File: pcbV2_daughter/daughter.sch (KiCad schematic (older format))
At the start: 27 parts, among them J3 Conn_01x03_Male, J6 Conn_01x03_Male

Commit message: finished v1 of daughter board
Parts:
- J6: footprint (none) -> Connector_PinHeader_2.54mm:PinHeader_1x03_P2.54mm_Vertical
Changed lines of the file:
@@
 F 0 "J6" H 15458 9581 50  0000 C CNN
 F 1 "Conn_01x03_Male" H 15458 9490 50  0000 C CNN
-F 2 "" H 15350 9300 50  0001 C CNN
+F 2 "Connector_PinHeader_2.54mm:PinHeader_1x03_P2.54mm_Vertical" H 15350 9300 50  0001 C CNN
 F 3 "~" H 15350 9300 50  0001 C CNN
 	1    15350 9300

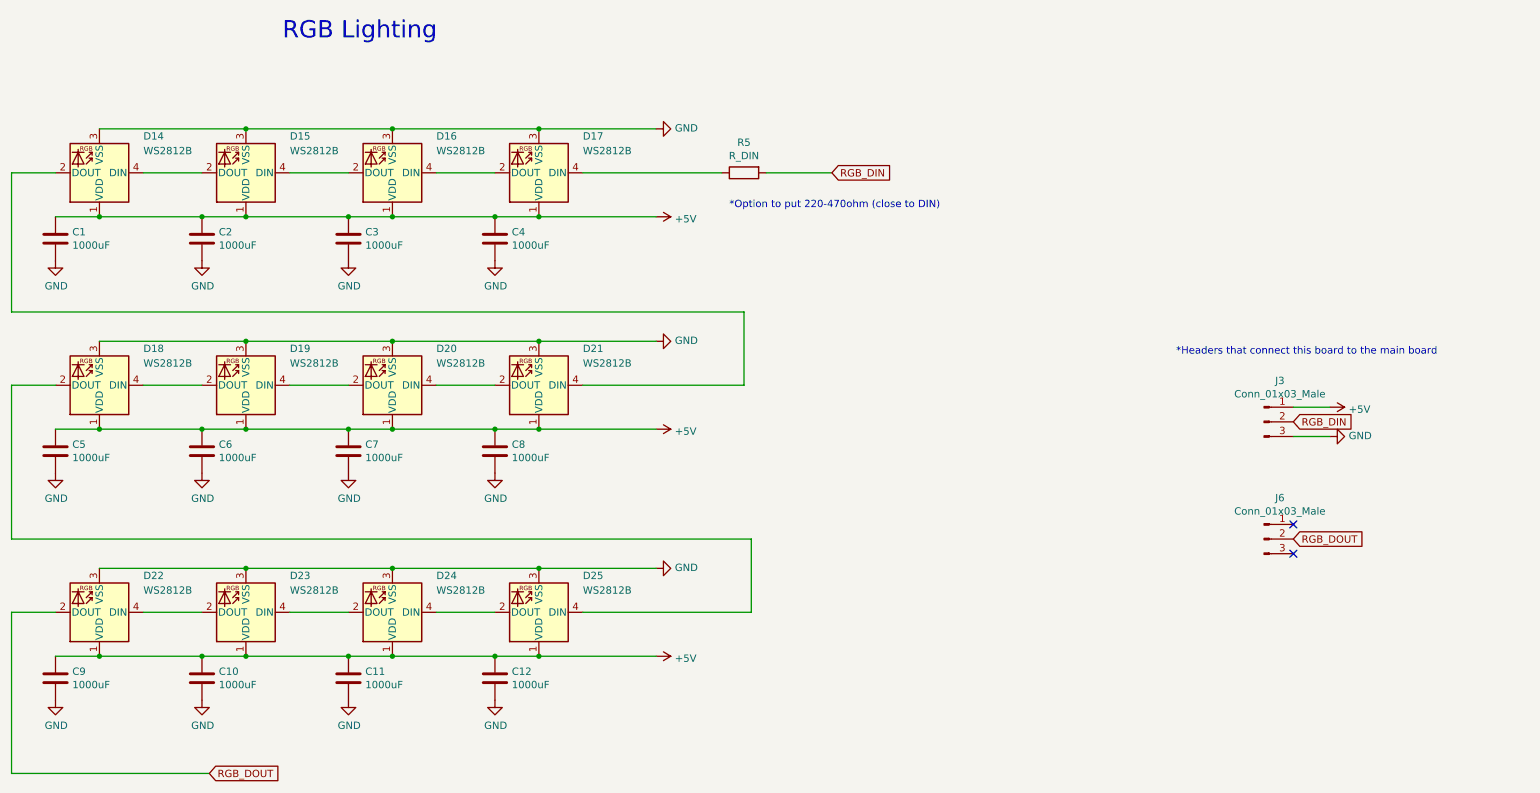
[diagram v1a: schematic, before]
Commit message: Prototype 1 Code changes (#9)
* started working on low priority work thread

* removed usb c

* setup a low priority worker thread that we can assign a bunch of menial tasks to

* added dip switch support

* started rewiring

* v2 layout

* edited layout, updated daughter board

* moved some labels around

* generated plots files

* added the ability to enable, disable and delete threads by handler ID

* added thread safety to the low priority work thread

* added documentation for dip switches

* finished adding thread safety code, fixed SPI dma ram waste usage

* update

* updated gerber files

* moved over lpwork into it's own module

* added signature to the codebase

* added more signatures

* updating daughter board to be more structurally safe

* generated gerber files

Co-authored-by: Jonathan Low <jwlow@uci.edu>
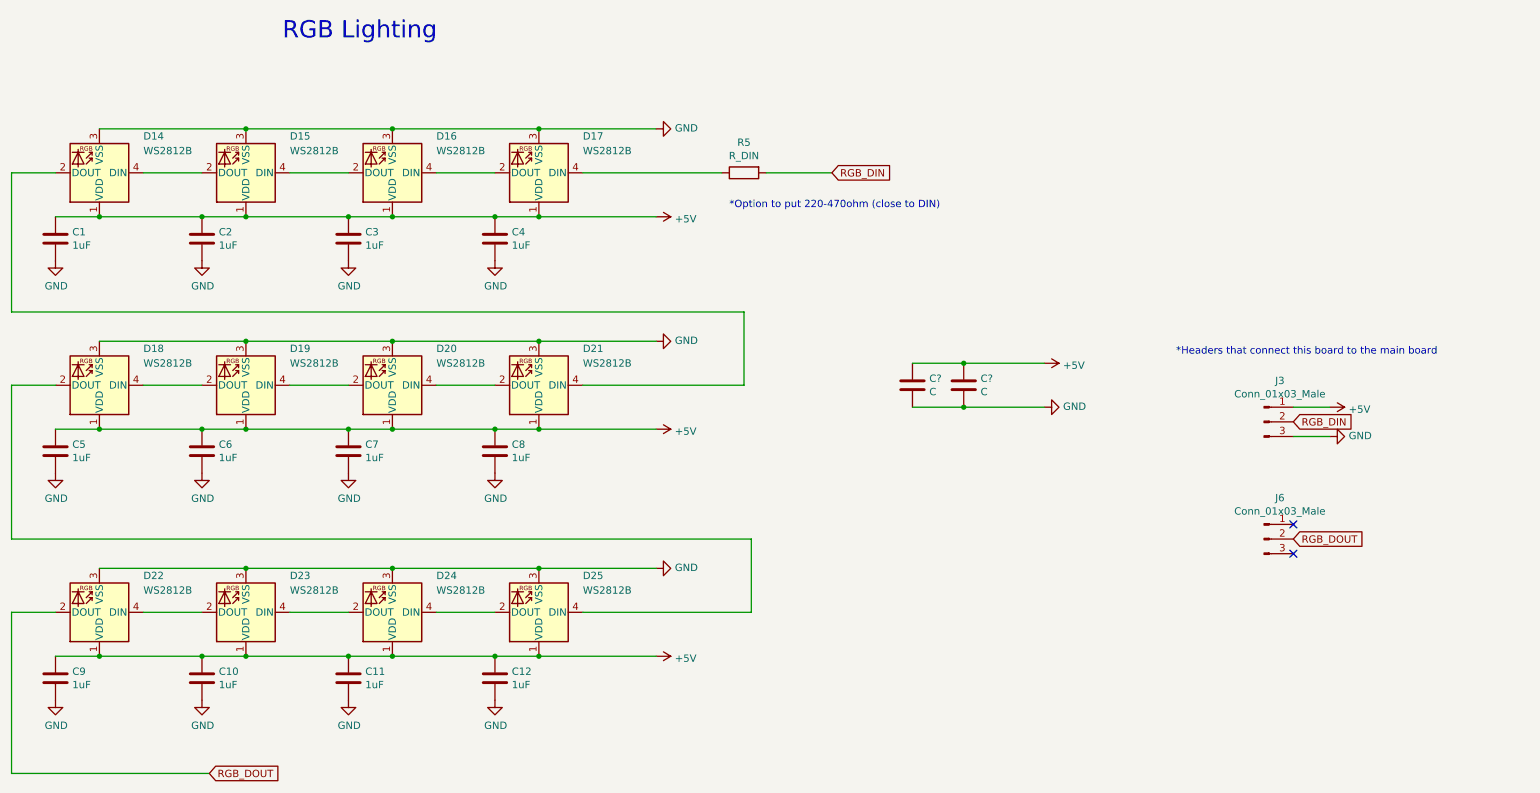
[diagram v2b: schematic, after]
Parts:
- added C? (x2): C, symbol Device:C
- C1, C10, C11, C12, C2, C3, C4, C5, C6, C7, C8, C9: value 1000uF -> 1uF
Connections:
- net +5V: now also C?.1, C?.1
- net GND: now also C?.2, C?.2
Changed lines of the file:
@@
 P 7100 7250
 F 0 "C1" H 7215 7296 50  0000 L CNN
-F 1 "1000uF" H 7215 7205 50  0000 L CNN
+F 1 "1uF" H 7215 7205 50  0000 L CNN
 F 2 "Capacitor_SMD:C_1206_3216Metric_Pad1.42x1.75mm_HandSolder" H 7138 7100 50  0001 C CNN
 F 3 "~" H 7100 7250 50  0001 C CNN
@@
 P 8100 7250
 F 0 "C2" H 8215 7296 50  0000 L CNN
-F 1 "1000uF" H 8215 7205 50  0000 L CNN
+F 1 "1uF" H 8215 7205 50  0000 L CNN
 F 2 "Capacitor_SMD:C_1206_3216Metric_Pad1.42x1.75mm_HandSolder" H 8138 7100 50  0001 C CNN
 F 3 "~" H 8100 7250 50  0001 C CNN
@@
 P 9100 7250
 F 0 "C3" H 9215 7296 50  0000 L CNN
-F 1 "1000uF" H 9215 7205 50  0000 L CNN
+F 1 "1uF" H 9215 7205 50  0000 L CNN
 F 2 "Capacitor_SMD:C_1206_3216Metric_Pad1.42x1.75mm_HandSolder" H 9138 7100 50  0001 C CNN
 F 3 "~" H 9100 7250 50  0001 C CNN
@@
 P 10100 7250
 F 0 "C4" H 10215 7296 50  0000 L CNN
-F 1 "1000uF" H 10215 7205 50  0000 L CNN
+F 1 "1uF" H 10215 7205 50  0000 L CNN
 F 2 "Capacitor_SMD:C_1206_3216Metric_Pad1.42x1.75mm_HandSolder" H 10138 7100 50  0001 C CNN
 F 3 "~" H 10100 7250 50  0001 C CNN
@@
 P 7100 8700
 F 0 "C5" H 7215 8746 50  0000 L CNN
-F 1 "1000uF" H 7215 8655 50  0000 L CNN
+F 1 "1uF" H 7215 8655 50  0000 L CNN
 F 2 "Capacitor_SMD:C_1206_3216Metric_Pad1.42x1.75mm_HandSolder" H 7138 8550 50  0001 C CNN
 F 3 "~" H 7100 8700 50  0001 C CNN
@@
 P 8100 8700
 F 0 "C6" H 8215 8746 50  0000 L CNN
-F 1 "1000uF" H 8215 8655 50  0000 L CNN
+F 1 "1uF" H 8215 8655 50  0000 L CNN
 F 2 "Capacitor_SMD:C_1206_3216Metric_Pad1.42x1.75mm_HandSolder" H 8138 8550 50  0001 C CNN
 F 3 "~" H 8100 8700 50  0001 C CNN
@@
 P 9100 8700
 F 0 "C7" H 9215 8746 50  0000 L CNN
-F 1 "1000uF" H 9215 8655 50  0000 L CNN
+F 1 "1uF" H 9215 8655 50  0000 L CNN
 F 2 "Capacitor_SMD:C_1206_3216Metric_Pad1.42x1.75mm_HandSolder" H 9138 8550 50  0001 C CNN
 F 3 "~" H 9100 8700 50  0001 C CNN
@@
 P 10100 8700
 F 0 "C8" H 10215 8746 50  0000 L CNN
-F 1 "1000uF" H 10215 8655 50  0000 L CNN
+F 1 "1uF" H 10215 8655 50  0000 L CNN
 F 2 "Capacitor_SMD:C_1206_3216Metric_Pad1.42x1.75mm_HandSolder" H 10138 8550 50  0001 C CNN
 F 3 "~" H 10100 8700 50  0001 C CNN
@@
 P 7100 10250
 F 0 "C9" H 7215 10296 50  0000 L CNN
-F 1 "1000uF" H 7215 10205 50  0000 L CNN
+F 1 "1uF" H 7215 10205 50  0000 L CNN
 F 2 "Capacitor_SMD:C_1206_3216Metric_Pad1.42x1.75mm_HandSolder" H 7138 10100 50  0001 C CNN
 F 3 "~" H 7100 10250 50  0001 C CNN
@@
 P 8100 10250
 F 0 "C10" H 8215 10296 50  0000 L CNN
-F 1 "1000uF" H 8215 10205 50  0000 L CNN
+F 1 "1uF" H 8215 10205 50  0000 L CNN
 F 2 "Capacitor_SMD:C_1206_3216Metric_Pad1.42x1.75mm_HandSolder" H 8138 10100 50  0001 C CNN
 F 3 "~" H 8100 10250 50  0001 C CNN
@@
 P 9100 10250
 F 0 "C11" H 9215 10296 50  0000 L CNN
-F 1 "1000uF" H 9215 10205 50  0000 L CNN
+F 1 "1uF" H 9215 10205 50  0000 L CNN
 F 2 "Capacitor_SMD:C_1206_3216Metric_Pad1.42x1.75mm_HandSolder" H 9138 10100 50  0001 C CNN
 F 3 "~" H 9100 10250 50  0001 C CNN
@@
 P 10100 10250
 F 0 "C12" H 10215 10296 50  0000 L CNN
-F 1 "1000uF" H 10215 10205 50  0000 L CNN
+F 1 "1uF" H 10215 10205 50  0000 L CNN
 F 2 "Capacitor_SMD:C_1206_3216Metric_Pad1.42x1.75mm_HandSolder" H 10138 10100 50  0001 C CNN
 F 3 "~" H 10100 10250 50  0001 C CNN
@@
 Text Notes 14750 8050 0    50   ~ 0
 *Headers that connect this board to the main board
+$Comp
+L Device:C C?
+U 1 1 5EFDA2EC
+P 12950 8250
+F 0 "C?" H 13065 8296 50  0000 L CNN
+F 1 "C" H 13065 8205 50  0000 L CNN
+F 2 "" H 12988 8100 50  0001 C CNN
+F 3 "~" H 12950 8250 50  0001 C CNN
+	1    12950 8250
+	1    0    0    -1
+$EndComp
+$Comp
+L Device:C C?
+U 1 1 5EFDC189
+P 13300 8250
+F 0 "C?" H 13415 8296 50  0000 L CNN
+F 1 "C" H 13415 8205 50  0000 L CNN
+F 2 "" H 13338 8100 50  0001 C CNN
+F 3 "~" H 13300 8250 50  0001 C CNN
+	1    13300 8250
+	1    0    0    -1
+$EndComp
+Wire Wire Line
+	12950 8100 13300 8100
+Connection ~ 13300 8100
+Wire Wire Line
+	13300 8100 13850 8100
+Wire Wire Line
+	12950 8400 13300 8400
+Connection ~ 13300 8400
+Wire Wire Line
+	13300 8400 13850 8400
+$Comp
+L power:GND #PWR?
+U 1 1 5EFE3AE9
+P 13850 8400
+F 0 "#PWR?" H 13850 8150 50  0001 C CNN
+F 1 "GND" V 13855 8272 50  0000 R CNN
+F 2 "" H 13850 8400 50  0001 C CNN
+F 3 "" H 13850 8400 50  0001 C CNN
+	1    13850 8400
+	0    -1   -1   0
+$EndComp
+$Comp
+L power:+5V #PWR?
+U 1 1 5EFE4903
+P 13850 8100
+F 0 "#PWR?" H 13850 7950 50  0001 C CNN
+F 1 "+5V" V 13865 8228 50  0000 L CNN
+F 2 "" H 13850 8100 50  0001 C CNN
+F 3 "" H 13850 8100 50  0001 C CNN
+	1    13850 8100
+	0    1    1    0
+$EndComp
 $EndSCHEMATC
